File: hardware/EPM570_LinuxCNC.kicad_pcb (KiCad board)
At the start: 2 copper layers, 122 x 92.2 mm, 232 parts, among them J1 PI Connector, J2 POWER +24V, J3 DIGITAL OUTPUTS, J4 JTAG, J5 DIGITAL INPUTS, J6 SERVO OUTPUTS, J7 SPI, J8 RS-485, U1 EPM570T100, U10 TLP291-4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

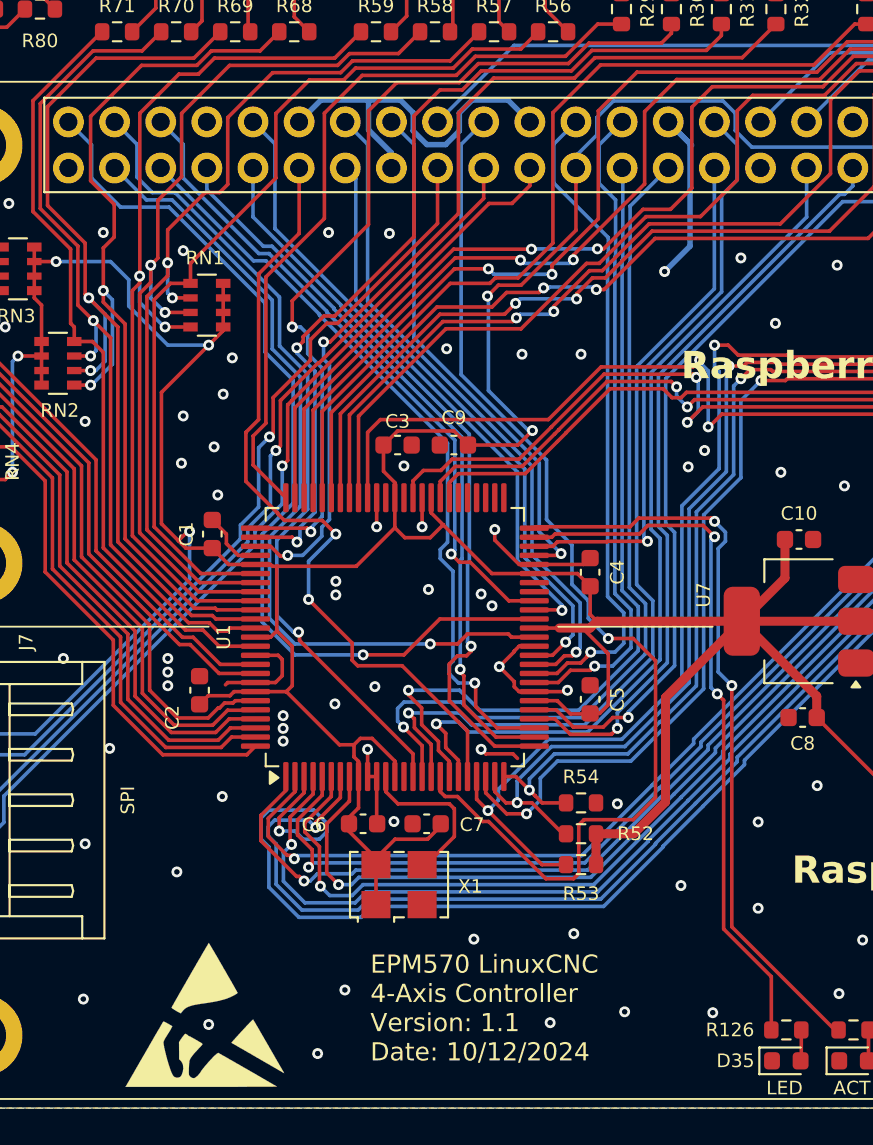
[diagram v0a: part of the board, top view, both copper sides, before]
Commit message: PCB fixes. Added pull down resistors.
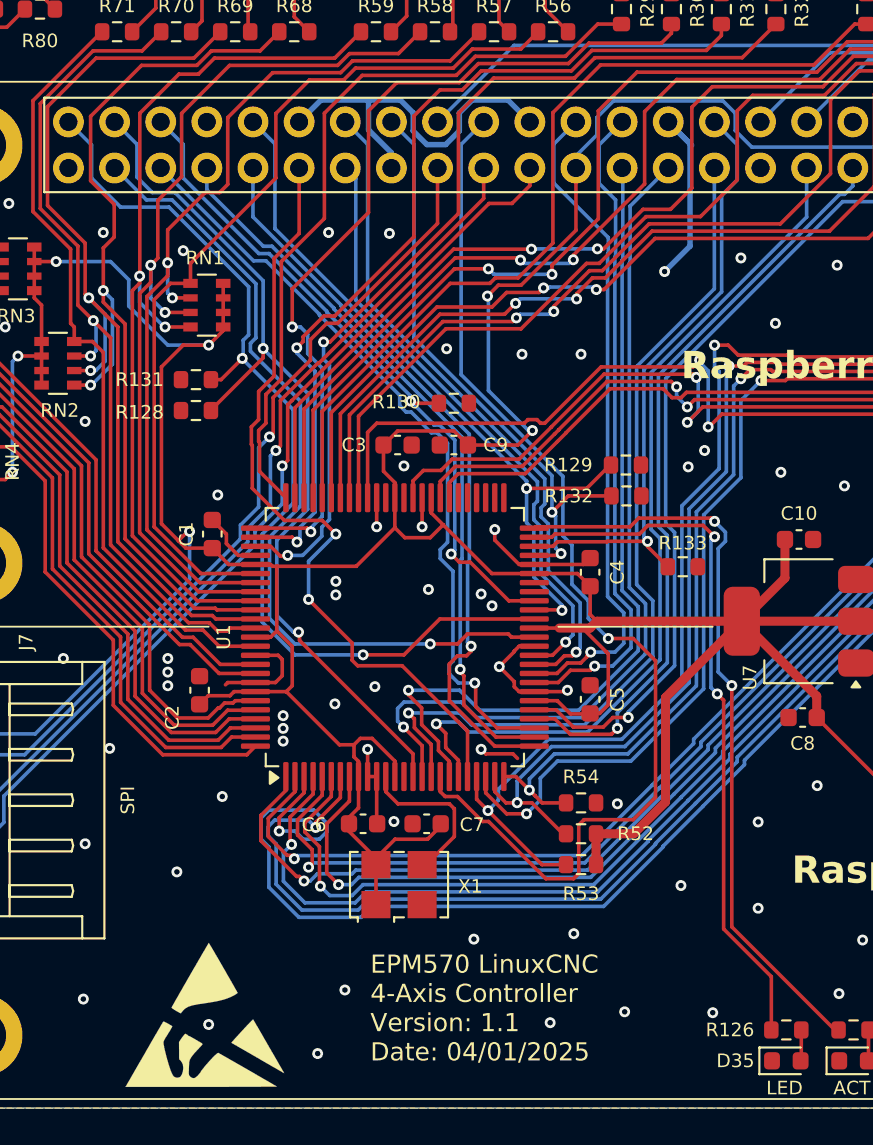
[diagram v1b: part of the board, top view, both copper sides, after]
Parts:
- added R128: 50K, Resistor_SMD:R_0603_1608Metric, F.Cu at (145.3, 78.6)
- added R129: 50K, Resistor_SMD:R_0603_1608Metric, F.Cu at (169.0, 81.6)
- added R130: 50K, Resistor_SMD:R_0603_1608Metric, F.Cu at (159.5, 78.2)
- added R131: 50K, Resistor_SMD:R_0603_1608Metric, F.Cu at (145.3, 76.9)
- added R132: 50K, Resistor_SMD:R_0603_1608Metric, F.Cu at (169.0, 83.3)
- added R133: 50K, Resistor_SMD:R_0603_1608Metric, F.Cu at (172.1, 87.2)
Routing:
- net /DATA_RW: track 35.5 -> 40.7 mm, vias 1 -> 2
- net /PULSE_BUFFER_LOCK: track 45.1 -> 49.8 mm, vias 1 -> 2
- net /PULSE_BUFFER_EMPTY: track 29.2 -> 32.8 mm, vias 1 -> 2
- net /DATA_ADDR: track 51.5 -> 54.0 mm, vias 1 -> 2
- net /INPUT_INTERRUPT: track 32.2 -> 34.0 mm
- net /DATA_READY: track 36.6 -> 38.3 mm, vias 1 -> 2
- net +3.3V: track 347.5 -> 348.3 mm
- net GND: vias 122 -> 117
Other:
- board text added: "EPM570 LinuxCNC 4-Axis Controller Version: 1.1 Date: 04/01/2025"
- board text removed: "EPM570 LinuxCNC 4-Axis Controller Version: 1.1 Date: 10/12/2024"
